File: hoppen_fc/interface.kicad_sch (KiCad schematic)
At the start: 60 parts, among them J10 PH2.0-3P, J11 PH2.0-3P, J12 GH1.25-4P, J13 GH1.25-4P, J15 GH1.25-4P, J16 GH1.25-2P, J17 GH1.25-2P, J18 GH1.25-5P, J2 PH2.0-3P, J3 GH1.25-4P, J5 GH1.25-4P, J6 PH2.0-3P, J7 GH1.25-8P, J8 GH1.25-6P, J9 PH2.0-3P, U15 LPW5209AB5F, U16 74AHCT1G125

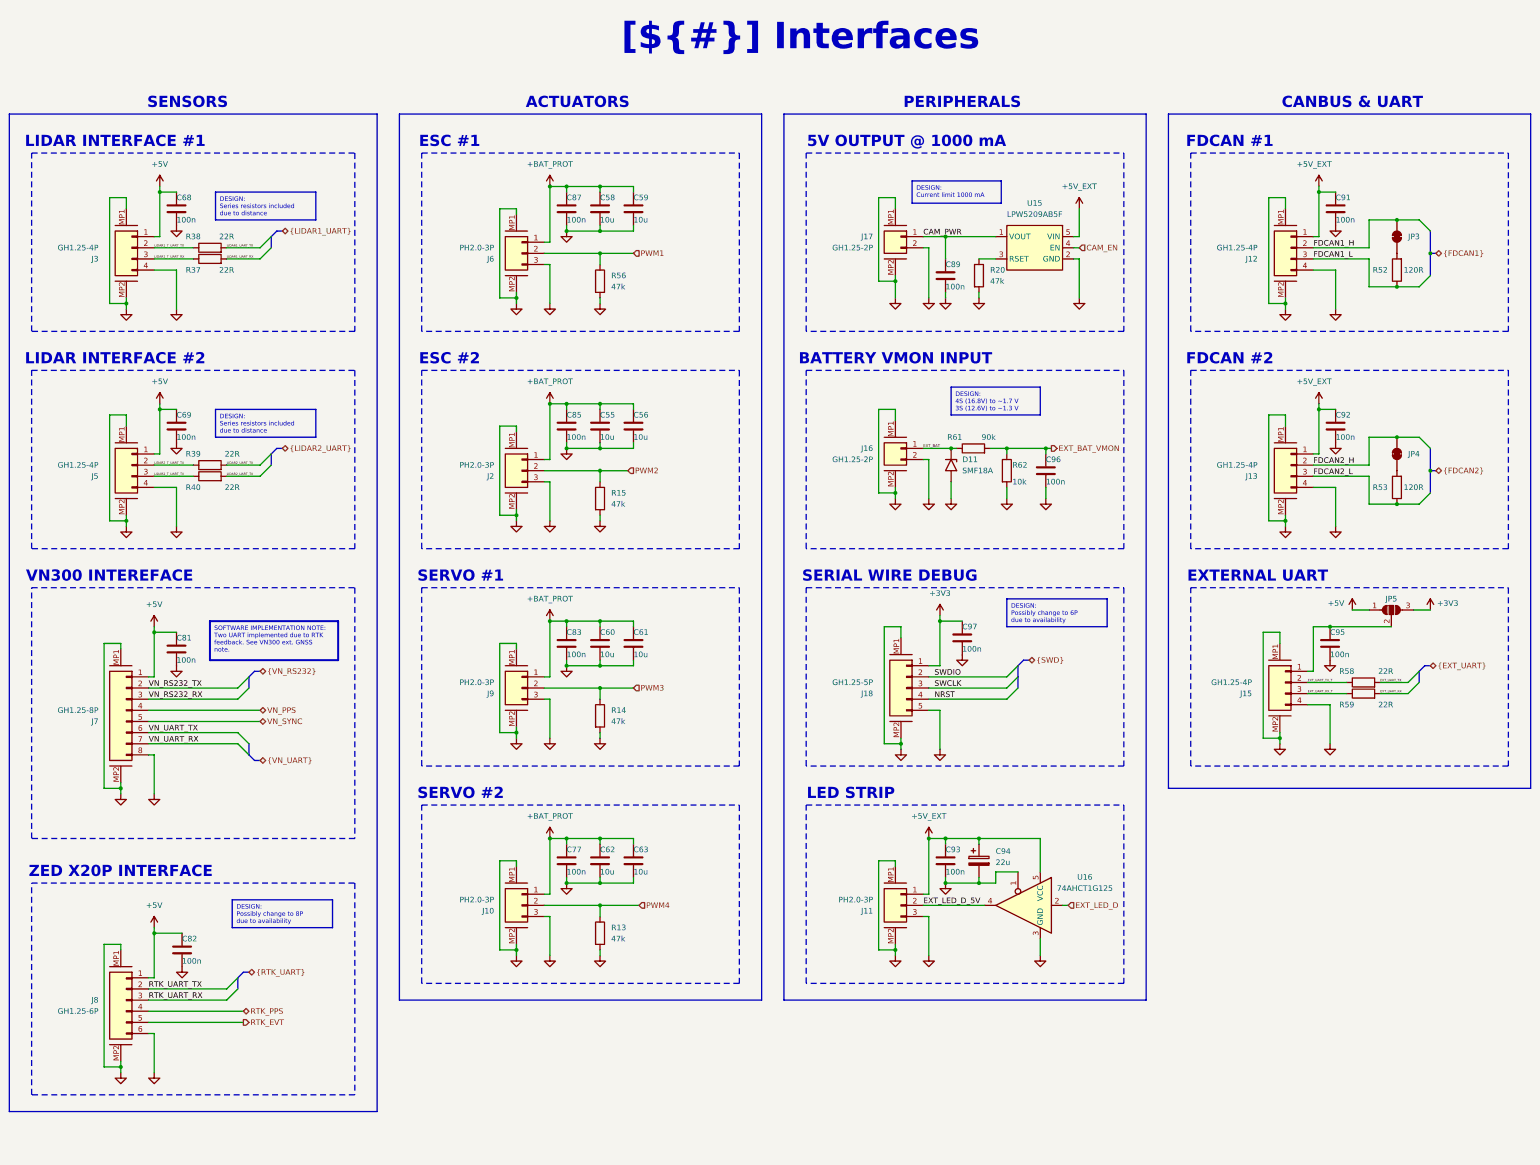
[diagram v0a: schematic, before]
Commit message: finished adding lcsc numbers
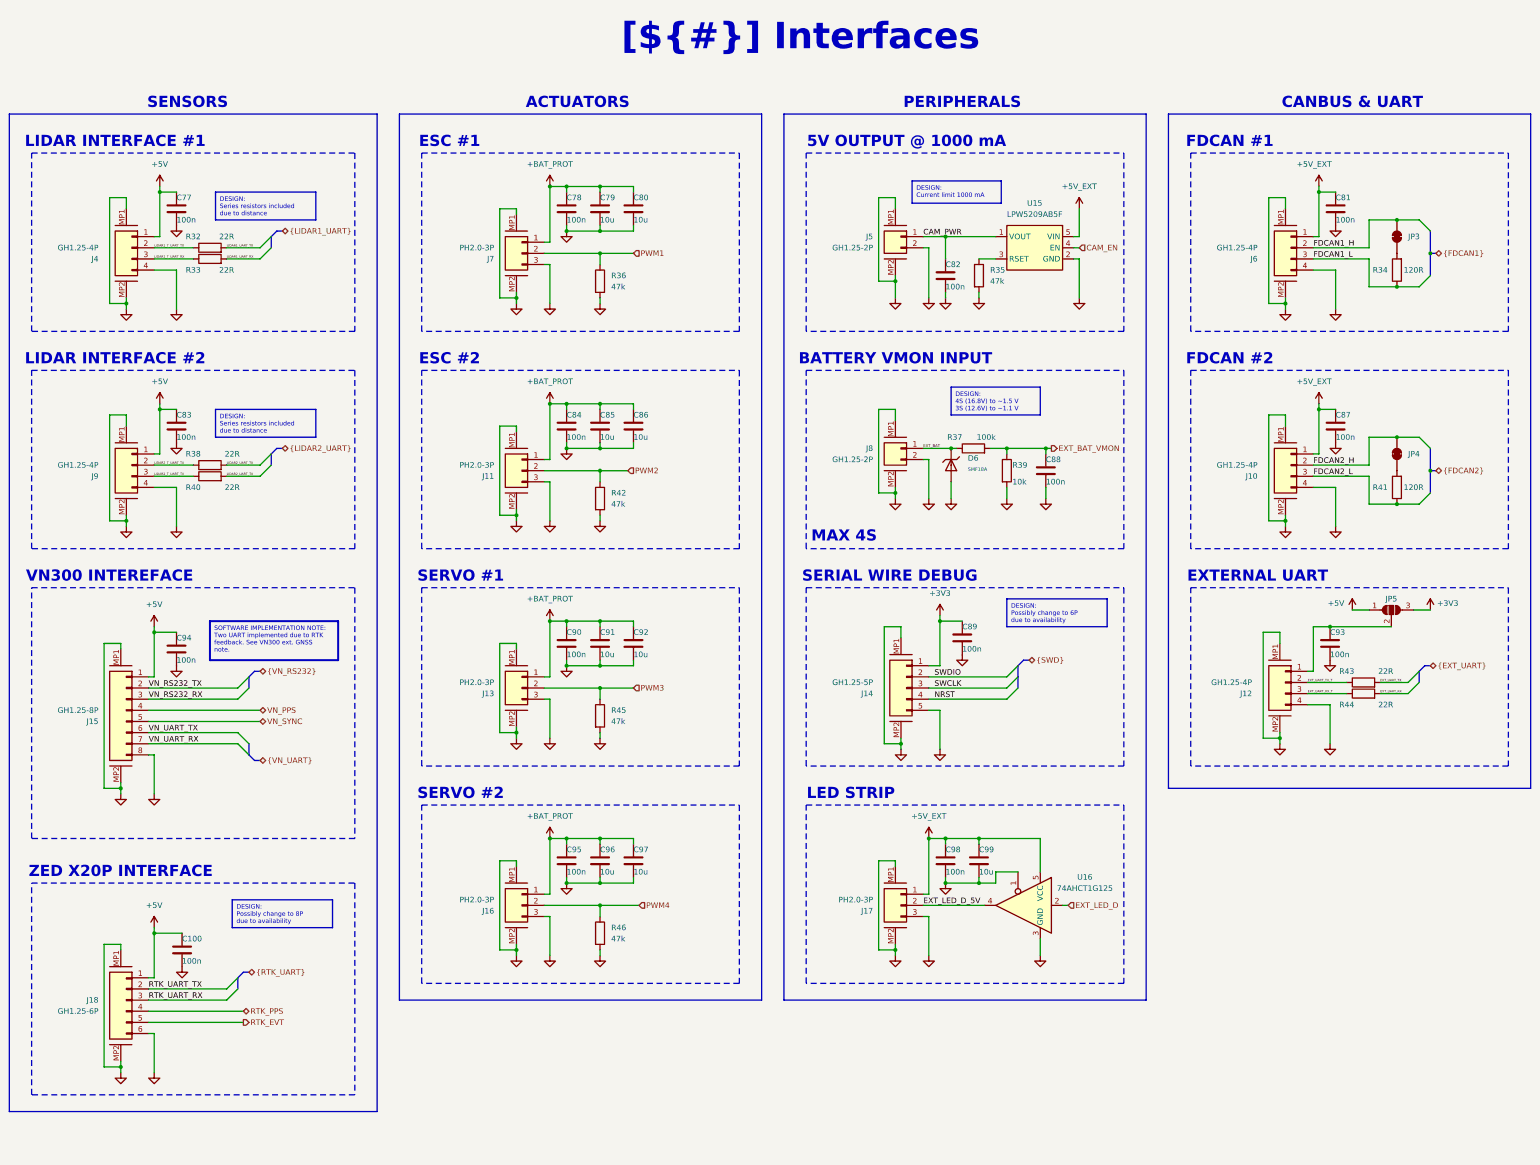
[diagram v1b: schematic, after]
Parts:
- removed C94: 22u, 0_capacitor_smd:CASE-B-3528-21, symbol Device:C_Polarized
- removed D11: SMF18A, Diode_SMD:D_SMF, symbol Diode:SMF18A
- added C99: 10u, 0_capacitor_smd:C_0805_2012Metric, symbol Device:C
- added D6: SMF18A, PCM_JLCPCB:D_SOD-123FL, symbol PCM_JLCPCB-Diodes:TVS-Uni,SMF18A
- C100: renamed from C82; LCSC (none) -> C307331
- C77: renamed from C68; LCSC (none) -> C307331
- C78: renamed from C87; LCSC (none) -> C307331
- C81: renamed from C91; LCSC (none) -> C307331
- C82: renamed from C89; LCSC (none) -> C307331
- C83: renamed from C69; LCSC (none) -> C307331
- C84: renamed from C85; LCSC (none) -> C307331
- C87: renamed from C92; LCSC (none) -> C307331
- C88: renamed from C96; LCSC (none) -> C307331
- C89: renamed from C97; LCSC (none) -> C307331
- C90: renamed from C83; LCSC (none) -> C307331
- C93: renamed from C95; LCSC (none) -> C307331
- C94: renamed from C81; footprint 0_resistor_smd:R_0603_1608Metric -> 0_capacitor_smd:C_0402_1005Metric; LCSC (none) -> C307331
- C95: renamed from C77; LCSC (none) -> C307331
- C98: renamed from C93; LCSC (none) -> C307331
- J10: renamed from J13; LCSC (none) -> C189895
- J11: renamed from J2; LCSC (none) -> C295747
- J12: renamed from J15; LCSC (none) -> C189895
- J13: renamed from J9; LCSC (none) -> C295747
- J14: renamed from J18; LCSC (none) -> C189896
- J15: renamed from J7; LCSC (none) -> C265111
- J16: renamed from J10; LCSC (none) -> C295747
- J17: renamed from J11; LCSC (none) -> C295747
- J18: renamed from J8; LCSC (none) -> C133065
- J4: renamed from J3; LCSC (none) -> C189895
- J5: renamed from J17; LCSC (none) -> C189893
- J6: renamed from J12; LCSC (none) -> C189895
- J7: renamed from J6; LCSC (none) -> C295747
- J8: renamed from J16; LCSC (none) -> C189893
- J9: renamed from J5; LCSC (none) -> C189895
- R32: renamed from R38; LCSC (none) -> C25092
- R33: renamed from R37; LCSC (none) -> C25092
- R34: renamed from R52; LCSC (none) -> C25079
- R35: renamed from R20; LCSC (none) -> C25792
- R36: renamed from R56; LCSC (none) -> C25792
- R37: renamed from R61; value 90k -> 100k; LCSC (none) -> C25741
- R38: renamed from R39; LCSC (none) -> C25092
- R39: renamed from R62; LCSC (none) -> C25744
- R40: LCSC (none) -> C25092
- R41: renamed from R53; LCSC (none) -> C25079
- R42: renamed from R15; LCSC (none) -> C25792
- R43: renamed from R58; LCSC (none) -> C25092
- R44: renamed from R59; LCSC (none) -> C25092
- R45: renamed from R14; LCSC (none) -> C25792
- R46: renamed from R13; LCSC (none) -> C25792
- U16: LCSC (none) -> C20617903
- renumbered C58 to C79, C59 to C80, C55 to C85, C56 to C86, C60 to C91, C61 to C92, C62 to C96, C63 to C97
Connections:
- net +5V_EXT: now also C99.1
- net EXT_BAT: now also D6.1
- net GND: now also C99.2, D6.2
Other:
- note added: "MAX 4S"

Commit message: ready for routing?
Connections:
- net FDCAN_T_1_J: now reaches JP3.1 (A), R34.2
- net FDCAN_T_2_J: now reaches JP4.1 (A), R41.2
- net EXT_UART_PWR: now reaches C93.1, J12.1 (Pin_1), JP5.2 (C)
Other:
- moved on the sheet: JP3, JP4, R34, R41

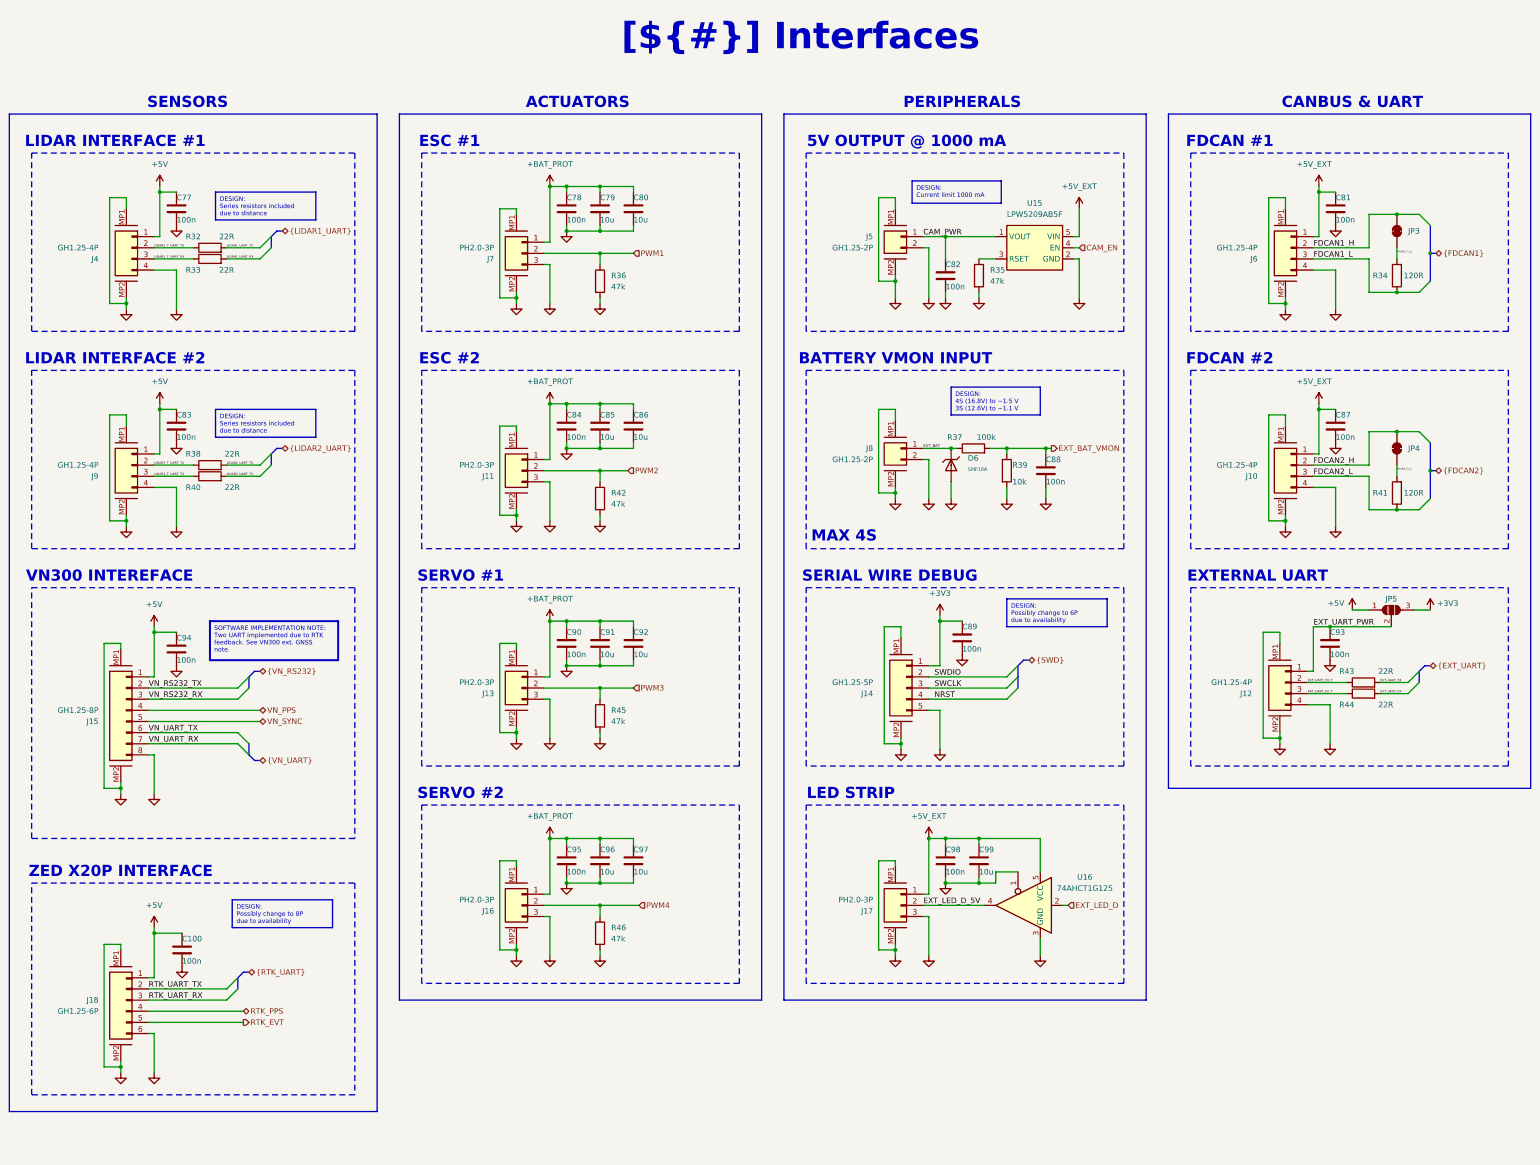
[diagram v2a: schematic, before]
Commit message: routing and adding rf module
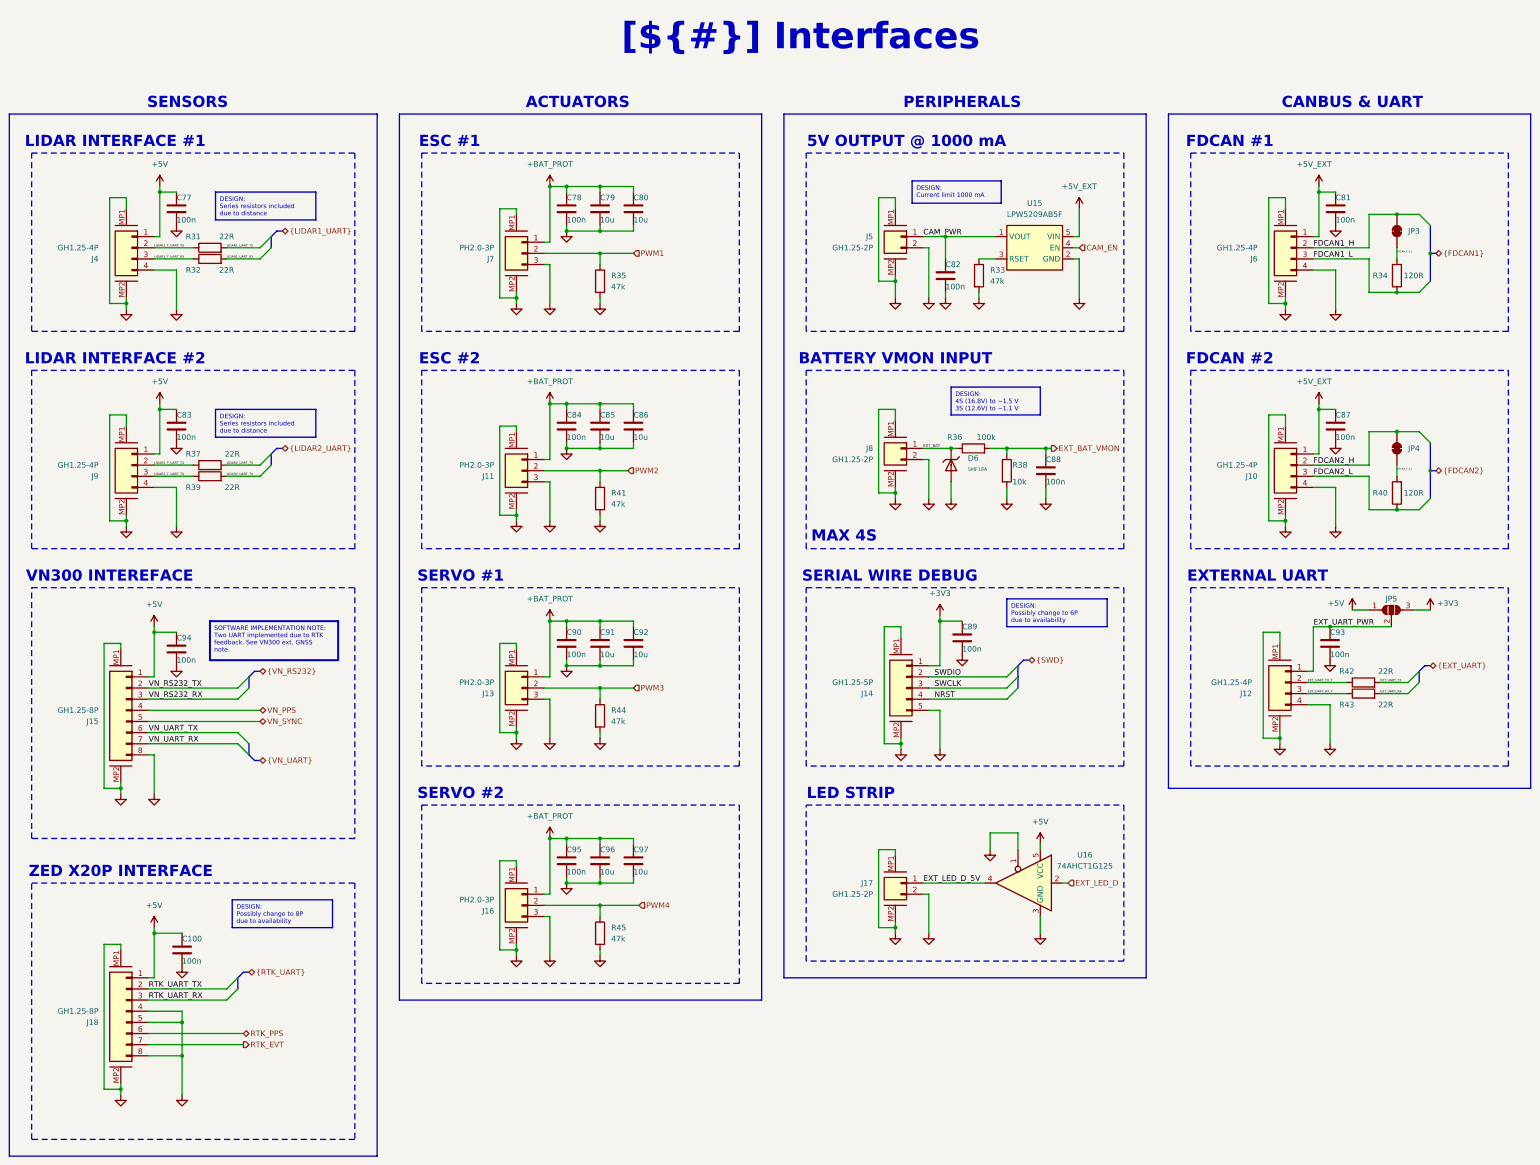
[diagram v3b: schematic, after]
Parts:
- removed C98: 100n, 0_capacitor_smd:C_0402_1005Metric, symbol Device:C
- removed C99: 10u, 0_capacitor_smd:C_0805_2012Metric, symbol Device:C
- removed J17: PH2.0-3P, 0_connectors:S3B-PH-SM4-TB-LF-SN, symbol 0_connectors:Conn_01x03_Mounting
- removed J18: GH1.25-6P, 0_connectors:SM06B-GHS-TB-LF-SN, symbol 0_connectors:Conn_01x06_Mounting
- added J17: GH1.25-2P, 0_connectors:SM02B-GHS-TB-LF-SN, symbol 0_connectors:Conn_01x02_Mounting
- added J18: GH1.25-8P, 0_connectors:SM08B-GHS-TB-LF-SN, symbol 0_connectors:Conn_01x08_Mounting
- renumbered R32 to R31, R33 to R32, R35 to R33, R36 to R35, R37 to R36, R38 to R37, R39 to R38, R40 to R39, R41 to R40, R42 to R41, R43 to R42, R44 to R43, R45 to R44, R46 to R45
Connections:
- net +5V: now also U16.5 (VCC), J18.1 (Pin_1)
- net +5V_EXT: no longer U16.5 (VCC)
- net EXT_LED_D_5V: now also J17.1 (Pin_1)
- net GND: now also J17.2 (Pin_2), J17.MP1, J17.MP2, J18.4 (Pin_4), J18.5 (Pin_5), J18.8 (Pin_8), J18.MP1, J18.MP2
- net RTK_EVT: now also J18.7 (Pin_7)
- net RTK_PPS: now also J18.6 (Pin_6)
- net RTK_UART_RX: now also J18.3 (Pin_3)
- net RTK_UART_TX: now also J18.2 (Pin_2)
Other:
- moved on the sheet: U16
